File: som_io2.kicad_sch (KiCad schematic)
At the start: 32 parts, among them J1 Hermaphroditic_Molex_203456-0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, J20 Tag-Connect_TC2050-IDC-NL_2x5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, Q28 PJE138K, U59 TXU0304BQAR, Y1 Oscillator_156.25MHz_SG3225EEN, Y4 Oscillator_100MHz_SG3225EEN

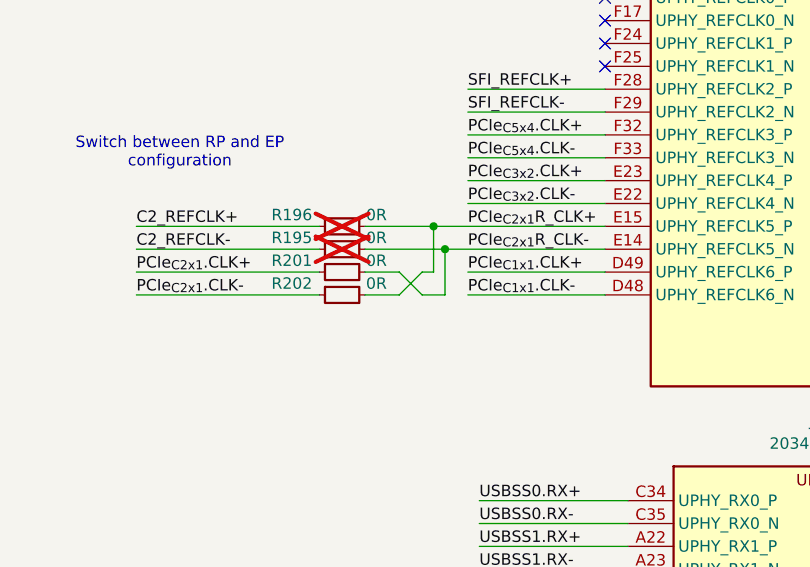
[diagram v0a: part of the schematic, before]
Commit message: [#83396] Route PCIe on expansion connector
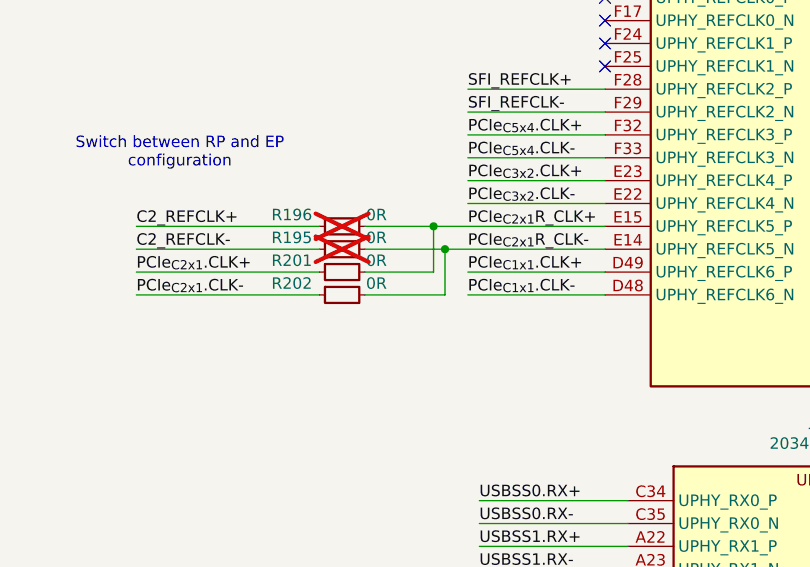
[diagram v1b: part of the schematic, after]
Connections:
- net PCIe_{C2x1}R_CLK+: now also R201.2; no longer R202.2
- net PCIe_{C2x1}R_CLK-: now also R202.2; no longer R201.2
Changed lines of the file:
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@@
 	(wire
 		(pts
-			(xy 52.07 82.55) (xy 55.88 82.55)
+			(xy 52.07 82.55) (xy 60.96 82.55)
 		)
 		(stroke
@@
 		)
 	)
-	(wire
-		(pts
-			(xy 55.88 80.01) (xy 58.42 82.55)
-		)
-		(stroke
-			(width 0)
-			(type default)
-		)
-	)
 	(bus
 		(pts
@@
 		)
 	)
-	(wire
-		(pts
-			(xy 55.88 82.55) (xy 58.42 80.01)
-		)
-		(stroke
-			(width 0)
-			(type default)
-		)
-	)
 	(bus
 		(pts
@@
 	(wire
 		(pts
-			(xy 58.42 82.55) (xy 60.96 82.55)
-		)
-		(stroke
-			(width 0)
-			(type default)
-		)
-	)
-	(wire
-		(pts
 			(xy 161.29 181.61) (xy 177.8 181.61)
 		)
@@
 	(wire
 		(pts
-			(xy 52.07 80.01) (xy 55.88 80.01)
+			(xy 52.07 80.01) (xy 59.69 80.01)
 		)
 		(stroke
@@
 		)
 		(stroke
-			(width 0)
-			(type default)
-		)
-	)
-	(wire
-		(pts
-			(xy 58.42 80.01) (xy 59.69 80.01)
-		)
-		(stroke

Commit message: [#83396] Route SFI
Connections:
- net SFI_REFCLK+: now also J1.F29 (UPHY_REFCLK2_N); no longer J1.F28 (UPHY_REFCLK2_P)
- net SFI_REFCLK-: now also J1.F28 (UPHY_REFCLK2_P); no longer J1.F29 (UPHY_REFCLK2_N)
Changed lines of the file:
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@@
 	(wire
 		(pts
-			(xy 63.5 62.23) (xy 78.74 62.23)
+			(xy 63.5 62.23) (xy 74.93 62.23)
 		)
 		(stroke
@@
 	(wire
 		(pts
+			(xy 77.47 62.23) (xy 78.74 62.23)
+		)
+		(stroke
+			(width 0)
+			(type default)
+		)
+	)
+	(wire
+		(pts
 			(xy 140.97 110.49) (xy 124.46 110.49)
 		)
@@
 	(wire
 		(pts
-			(xy 63.5 59.69) (xy 78.74 59.69)
+			(xy 63.5 59.69) (xy 74.93 59.69)
 		)
 		(stroke
@@
 		)
 	)
+	(wire
+		(pts
+			(xy 74.93 59.69) (xy 77.47 62.23)
+		)
+		(stroke
+			(width 0)
+			(type default)
+		)
+	)
 	(bus
 		(pts
@@
 	(wire
 		(pts
+			(xy 74.93 62.23) (xy 77.47 59.69)
+		)
+		(stroke
+			(width 0)
+			(type default)
+		)
+	)
+	(wire
+		(pts
 			(xy 64.77 156.21) (xy 81.28 156.21)
 		)
@@
 	(wire
 		(pts
+			(xy 77.47 59.69) (xy 78.74 59.69)
+		)
+		(stroke
+			(width 0)
+			(type default)
+		)
+	)
+	(wire
+		(pts
 			(xy 161.29 111.76) (xy 177.8 111.76)
 		)
@@
 		(polyline
 			(pts
-				(xy 60.96 57.15) (xy 60.96 62.865) (xy 76.835 62.865) (xy 76.835 57.15)
+				(xy 60.96 57.15) (xy 60.96 62.865) (xy 78.105 62.865) (xy 78.105 57.15)
 			)
 			(stroke

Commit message: [#83396] Update all symbols from library and clear all ERC errors
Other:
- moved on the sheet: J1B, J1C, J1E, J1F, J1G, J1J

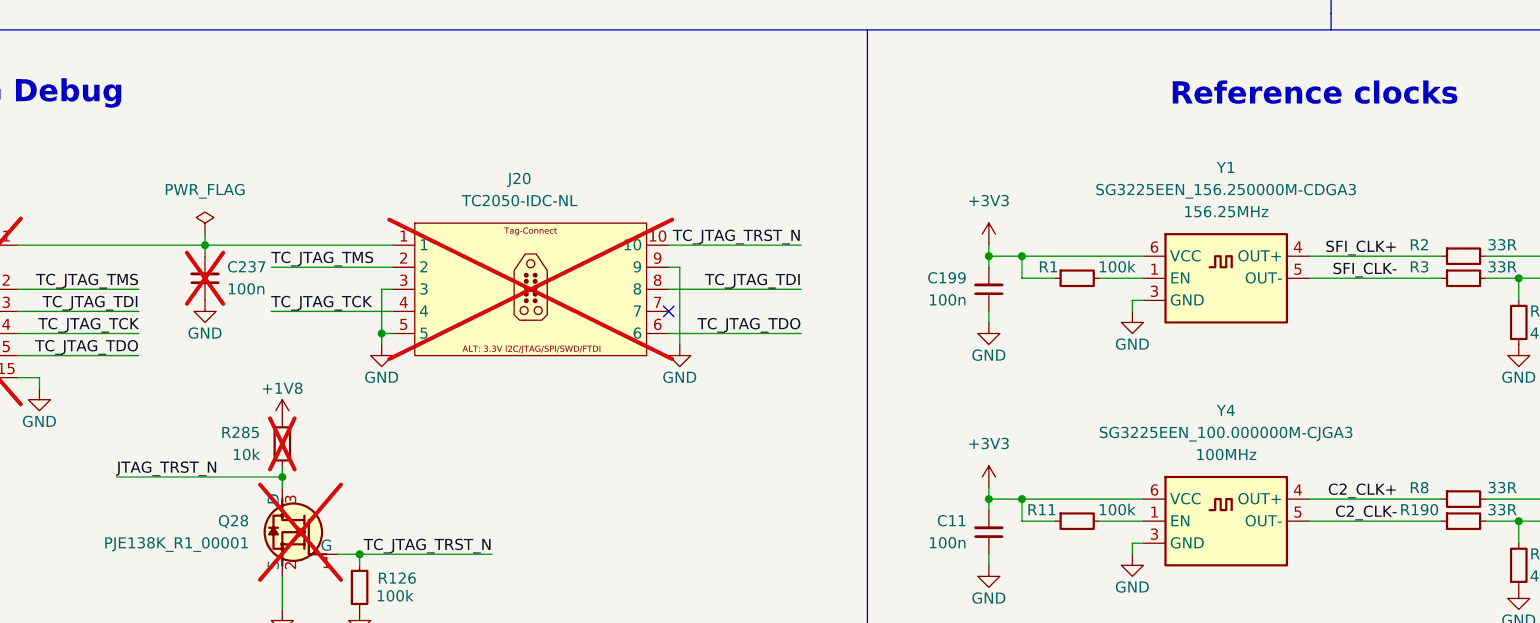
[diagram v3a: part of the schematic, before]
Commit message: [#83396] Implement small post review fixes eg. correct LED resistor values, update sheet table, delete four wire connections
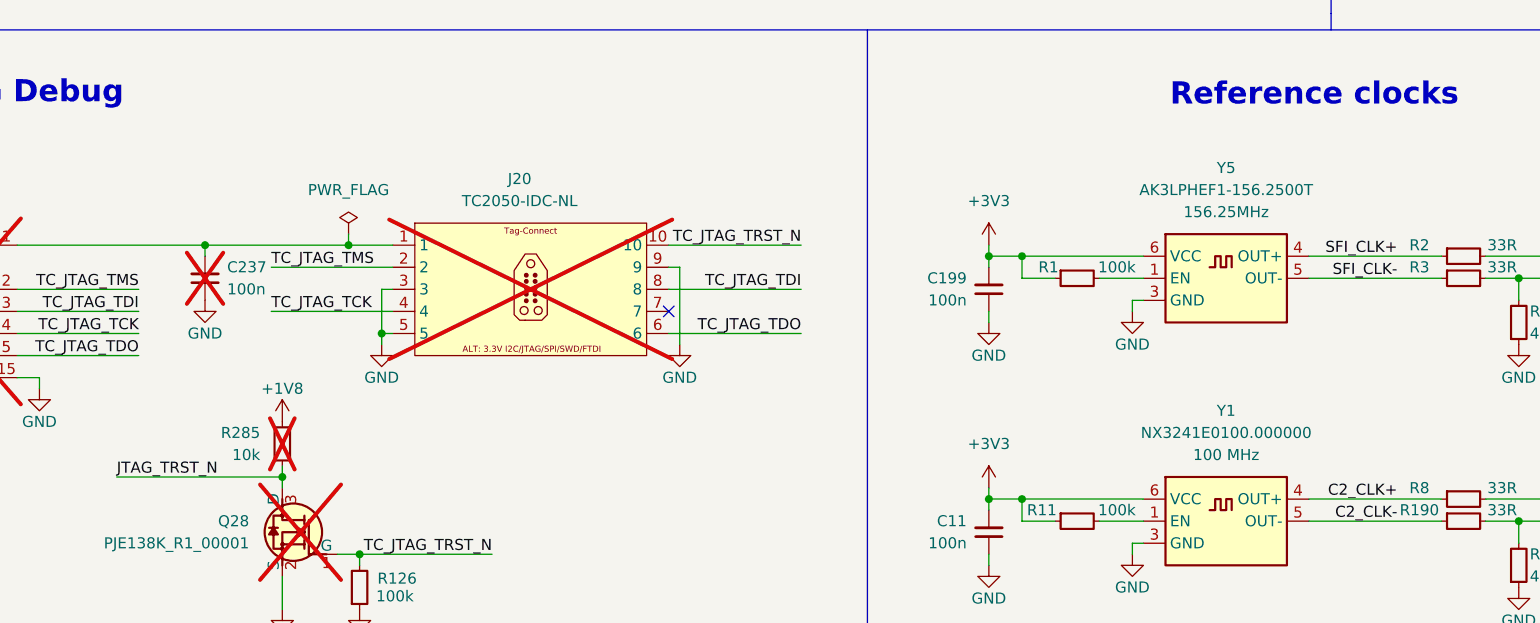
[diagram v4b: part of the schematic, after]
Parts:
- removed Y1: Oscillator_156.25MHz_SG3225EEN, antmicro-footprints:Oscillator_SMD_Epson_SG3225EEN_3.2x2.5x1.2mm, symbol antmicroOscillators:Oscillator_156.25MHz_SG3225EEN
- removed Y4: Oscillator_100MHz_SG3225EEN, antmicro-footprints:Oscillator_SMD_Epson_SG3225EEN_3.2x2.5x1.2mm, symbol antmicroOscillators:Oscillator_100MHz_SG3225EEN
- added Y1: Oscillator_100MHz_NX324, antmicro-footprints:Oscillator_SMD_Abracon_AX3_3.2x2.5x1mm, symbol antmicroOscillators:Oscillator_100MHz_NX324
- added Y5: Oscillator_156.25MHz_AK3LPHEF1, antmicro-footprints:Oscillator_SMD_Abracon_AK3LPHEF1_3.2x2.5x1mm, symbol antmicroOscillators:Oscillator_156.25MHz_AK3LPHEF1
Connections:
- net +3V3: now also Y1.6 (VCC), Y5.6 (VCC)
- net C2_CLK+: now also Y1.4 (OUT+)
- net C2_CLK-: now also Y1.5 (OUT-)
- net GND: now also Y1.3 (GND), Y5.3 (GND)
- net SFI_CLK+: now also Y5.4 (OUT+)
- net SFI_CLK-: now also Y5.5 (OUT-)
- net at R1.2: now also Y5.1 (EN)
- net at R11.2: now also Y1.1 (EN)

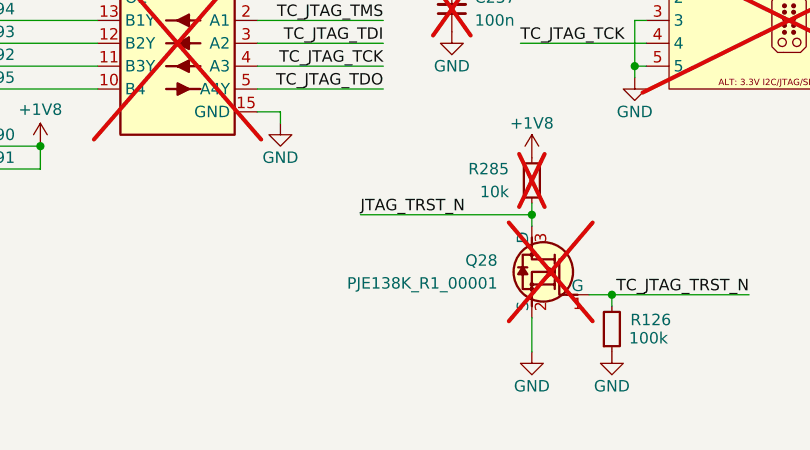
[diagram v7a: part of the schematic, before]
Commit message: [#85326] Add reviewers suggestions; Unify BOM
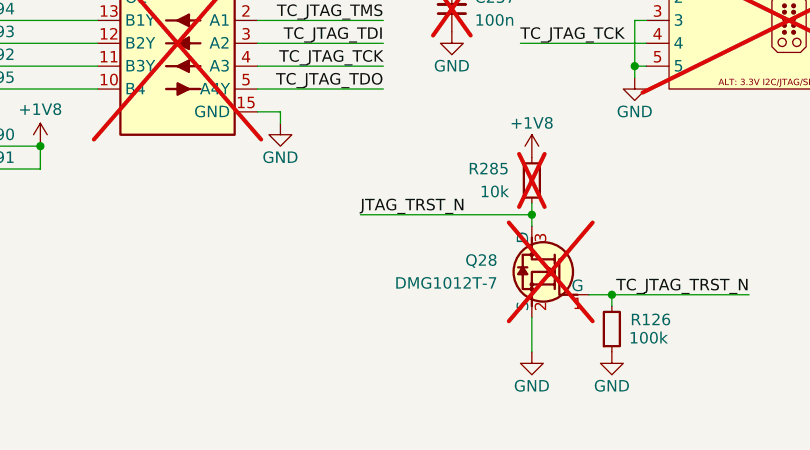
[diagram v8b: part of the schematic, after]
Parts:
- C237, C238: value C_100n_50V_X8L_0402 -> C_100n_0402; symbol antmicroCapacitors0402:C_100n_50V_X8L_0402 -> antmicroCapacitors0402:C_100n_0402; Dielectric X8L -> X5R; MPN GCM155L8EH104KE07D -> GRM155R61H104KE14D
- Q28: value PJE138K -> DMG1012T-7; symbol antmicroTransistorsFETsMOSFETsSingle:PJE138K -> antmicroTransistorsFETsMOSFETsSingle:DMG1012T-7; MPN PJE138K_R1_00001 -> DMG1012T-7; Manufacturer PANJIT -> Diodes Incorporated; now left out of the parts list
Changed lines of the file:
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@@
 	)
 	(symbol
-		(lib_id "antmicroCapacitors0402:C_100n_50V_X8L_0402")
+		(lib_id "antmicroCapacitors0402:C_100n_0402")
 		(at 66.04 229.87 270)
 		(mirror x)
@@
 			)
 		)
-		(property "Value" "C_100n_50V_X8L_0402"
+		(property "Value" "C_100n_0402"
 			(at 43.18 214.63 0)
 			(effects
@@
 			)
 		)
-		(property "Datasheet" "https://www.murata.com/products/productdetail?partno=GCM155L8EH104KE07%23"
+		(property "Datasheet" "https://www.murata.com/products/productdetail?partno=GRM155R61H104KE14%23"
 			(at 38.1 214.63 0)
 			(effects
@@
 			)
 		)
-		(property "Description" "SMD Multilayer Ceramic Capacitor, 100nF, 50V, 0402, ±10%, X8L"
+		(property "Description" "SMD Multilayer Ceramic Capacitor, 0.1 µF, 50 V, 0402 [1005 Metric], ± 10%, X5R, GRM Series"
 			(at 66.04 229.87 0)
 			(effects
@@
 			)
 		)
-		(property "MPN" "GCM155L8EH104KE07D"
+		(property "MPN" "GRM155R61H104KE14D"
 			(at 35.56 214.63 0)
 			(effects
@@
 			)
 		)
-		(property "Dielectric" "X8L"
+		(property "Dielectric" "X5R"
 			(at 53.34 214.63 0)
 			(effects
@@
 	)
 	(symbol
-		(lib_id "antmicroCapacitors0402:C_100n_50V_X8L_0402")
+		(lib_id "antmicroCapacitors0402:C_100n_0402")
 		(at 115.57 240.03 90)
 		(unit 1)
@@
 			)
 		)
-		(property "Value" "C_100n_50V_X8L_0402"
+		(property "Value" "C_100n_0402"
 			(at 138.43 224.79 0)
 			(effects
@@
 			)
 		)
-		(property "Datasheet" "https://www.murata.com/products/productdetail?partno=GCM155L8EH104KE07%23"
+		(property "Datasheet" "https://www.murata.com/products/productdetail?partno=GRM155R61H104KE14%23"
 			(at 143.51 224.79 0)
 			(effects
@@
 			)
 		)
-		(property "Description" "SMD Multilayer Ceramic Capacitor, 100nF, 50V, 0402, ±10%, X8L"
+		(property "Description" "SMD Multilayer Ceramic Capacitor, 0.1 µF, 50 V, 0402 [1005 Metric], ± 10%, X5R, GRM Series"
 			(at 115.57 240.03 0)
 			(effects
@@
 			)
 		)
-		(property "MPN" "GCM155L8EH104KE07D"
+		(property "MPN" "GRM155R61H104KE14D"
 			(at 146.05 224.79 0)
 			(effects
@@
 			)
 		)
-		(property "Dielectric" "X8L"
+		(property "Dielectric" "X5R"
 			(at 128.27 224.79 0)
 			(effects
@@
 	)
 	(symbol
-		(lib_id "antmicroTransistorsFETsMOSFETsSingle:PJE138K")
+		(lib_id "antmicroTransistorsFETsMOSFETsSingle:DMG1012T-7")
 		(at 130.81 269.24 0)
 		(mirror y)
 		(unit 1)
 		(exclude_from_sim no)
-		(in_bom yes)
+		(in_bom no)
 		(on_board yes)
 		(dnp yes)
@@
 			)
 		)
-		(property "Value" "PJE138K"
+		(property "Value" "DMG1012T-7"
 			(at 107.95 278.13 0)
 			(effects
@@
 			)
 		)
-		(property "Datasheet" "https://www.mouser.com/datasheet/2/1057/PJE138K-1876698.pdf"
+		(property "Datasheet" "https://www.diodes.com/assets/Datasheets/ds31783.pdf"
 			(at 107.95 283.21 0)
 			(effects
@@
 			)
 		)
-		(property "Description" "MOSFET, N Channel, 50V, 0.35A, 4.5 ohm, SOT-523, Surface Mount"
+		(property "Description" "Power MOSFET, N Channel, 20 V, 630 mA, 0.3 ohm, SOT-523, Surface Mount"
 			(at 107.95 294.894 0)
 			(effects
@@
 			)
 		)
-		(property "MPN" "PJE138K_R1_00001"
+		(property "MPN" "DMG1012T-7"
 			(at 120.65 267.97 0)
 			(effects
@@
 			)
 		)
-		(property "Manufacturer" "PANJIT"
+		(property "Manufacturer" "Diodes Incorporated"
 			(at 107.95 288.29 0)
 			(effects
